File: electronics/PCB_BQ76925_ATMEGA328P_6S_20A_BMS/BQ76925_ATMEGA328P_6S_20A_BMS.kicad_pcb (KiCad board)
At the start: 2 copper layers, 47 x 90 mm, 79 parts, among them J1 Conn_01x01, J2 Conn_01x01, J3 Conn_01x09, J4 Conn_01x02, J5 Conn_02x03, J6 Conn_01x04, Q1 BC817, Q2 IRFB4110, Q3 IRFB4110, Q4 IRFB4110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

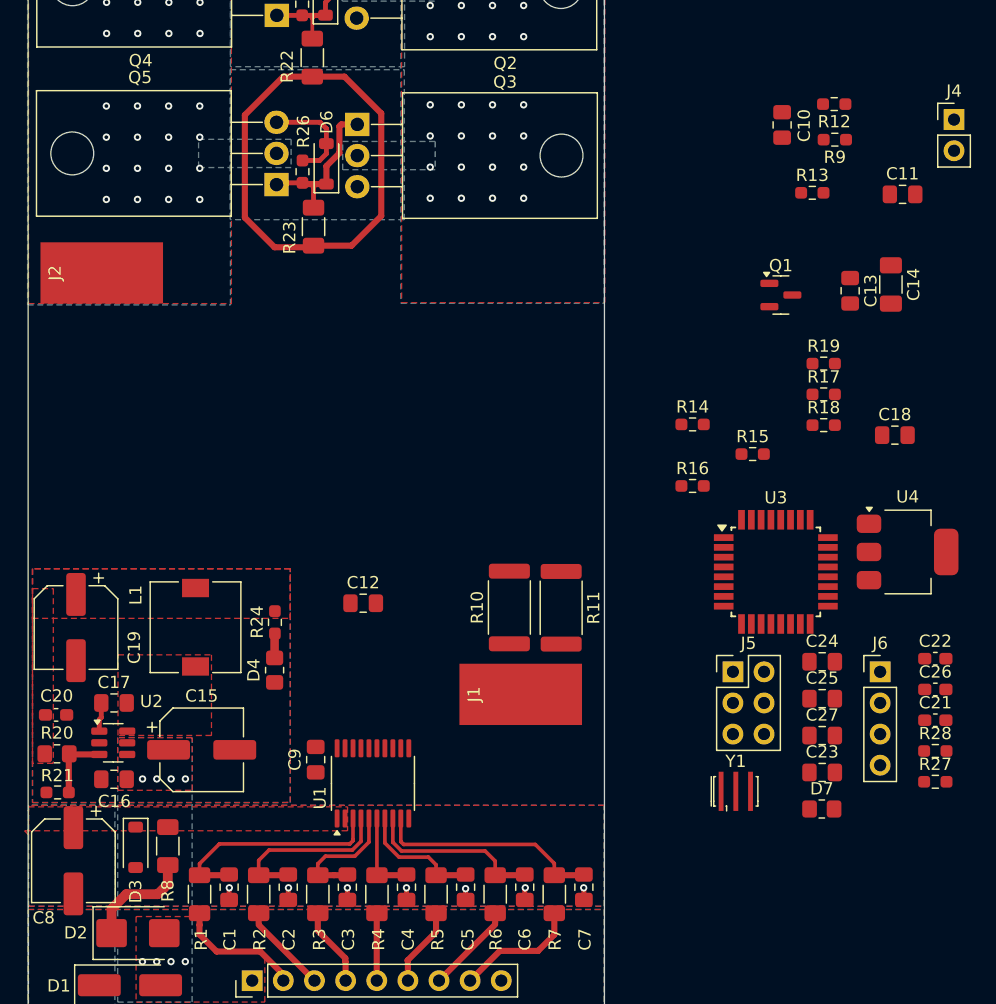
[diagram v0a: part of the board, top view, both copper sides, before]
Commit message: routing issue analog pins parallel routing and more length need to plan
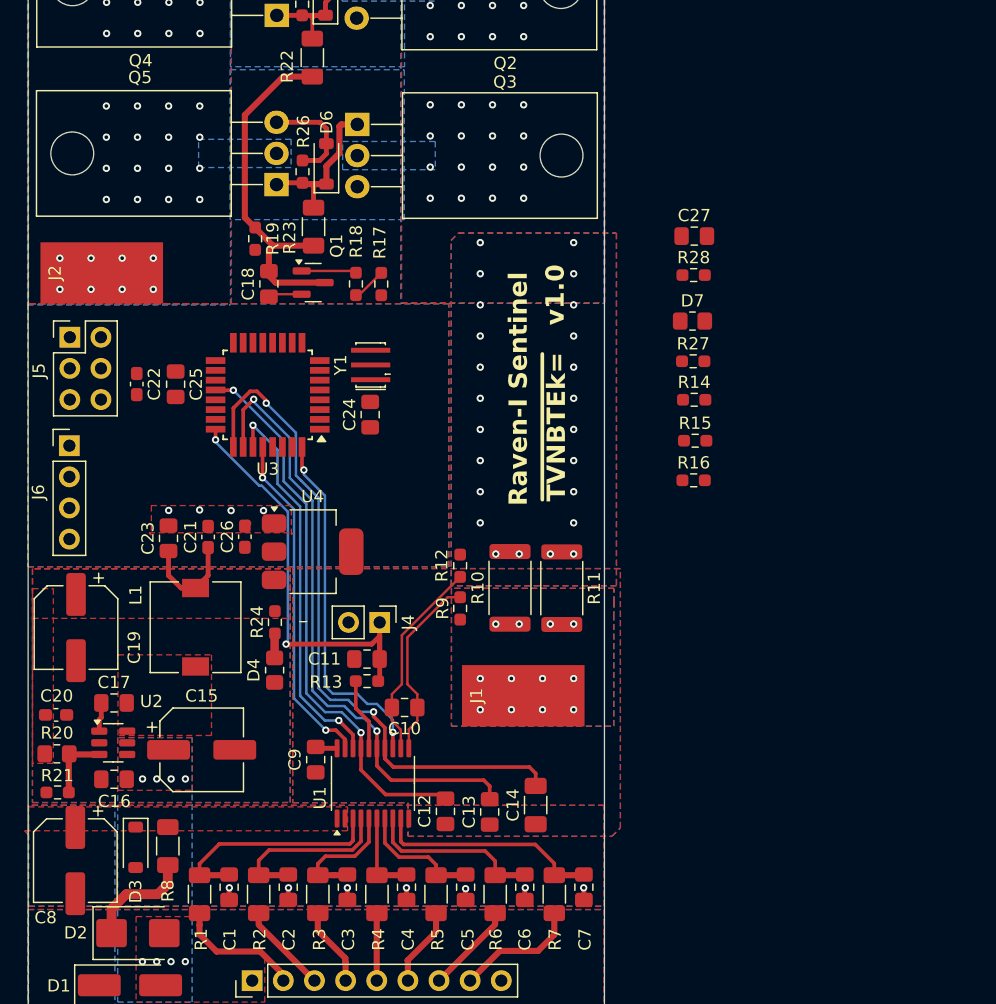
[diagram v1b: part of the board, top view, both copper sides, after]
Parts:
- moved C22 68.9 mm to (124.4, 87.7), turned to -90 degrees
- moved J6 68.7 mm to (118.9, 92.8)
- moved J4 62.3 mm to (144.2, 107.2), turned to -90 degrees
- moved C21 61.2 mm to (130.2, 100.2), turned to 90 degrees
- moved J5 60.6 mm to (118.9, 83.9)
- moved C25 58.6 mm to (127.5, 87.8), turned to -90 degrees
- moved C11 57.8 mm to (143.2, 110.2)
- moved C26 57.7 mm to (133.2, 100.2), turned to 90 degrees
- moved C23 56.6 mm to (127.0, 100.3), turned to 90 degrees
- moved C10 56.6 mm to (146.2, 114.1), turned to 180 degrees
- moved R13 53.9 mm to (143.2, 112.0), turned to 180 degrees
- moved C18 52.5 mm to (135.2, 79.6), turned to -90 degrees
- moved C13 51.7 mm to (153.2, 122.6), turned to 90 degrees
- moved C14 51.4 mm to (156.9, 122.1), turned to 90 degrees
- moved R9 48.9 mm to (150.8, 106.0), turned to 90 degrees
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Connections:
- net Net-(U1-SENSEN) renamed /24V 6 Cell Monitoring/A+
- net Net-(U1-SENSEP) renamed /24V 6 Cell Monitoring/A-
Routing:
- net /24V 6 Cell Monitoring/VIOUT: track 0.00 -> 55.3 mm, vias 0 -> 2
- net /24V 6 Cell Monitoring/VCOUT: track 0.00 -> 50.5 mm, vias 0 -> 2
- net /24V 6 Cell Monitoring/VREF: track 0.00 -> 45.4 mm, vias 0 -> 2
- net /24V 6 Cell Monitoring/VTB: track 0.00 -> 34.8 mm, vias 0 -> 2
- net /24V 6 Cell Monitoring/SDA: track 0.00 -> 32.2 mm, vias 0 -> 2
- net /24V 6 Cell Monitoring/ALERT: track 0.00 -> 29.3 mm, vias 0 -> 2
- net /24V 6 Cell Monitoring/SCL: track 0.00 -> 27.9 mm, vias 0 -> 2
- net /24V 6 Cell Monitoring/A-: track 0.00 -> 16.6 mm
- net /24V 6 Cell Monitoring/A+: track 0.00 -> 15.3 mm
- net Net-(Q1-C): track 43.6 -> 29.1 mm
- net +12V: track 0.00 -> 8.35 mm
- net Net-(U1-VTB): track 0.00 -> 5.92 mm
- net Net-(Q1-B): track 0.00 -> 4.49 mm
- net GND: track 6.88 -> 9.98 mm, vias 7 -> 11
- net /MCU/SW: track 0.00 -> 2.82 mm
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- added copper zone on F.Cu, net +5V
- added copper zone on B.Cu, net /24V 6 Cell Monitoring/BAT-
- added copper zone on F.Cu, net /24V 6 Cell Monitoring/BAT-
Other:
- board text added: "Raven-I Sentinel"
- board text added: "v1.0"
- board text added: "~{TVNBTEk=}"

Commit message: pcb placement and 90 percent routed
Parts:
- moved R14 45.8 mm to (137.0, 120.9), turned to 180 degrees
- moved C27 43.1 mm to (154.1, 115.8)
- moved J6 42.1 mm to (158.3, 107.6)
- moved R15 41.8 mm to (137.0, 118.0), turned to 180 degrees
- moved D7 40.4 mm to (131.5, 95.5), turned to -90 degrees
- moved R28 38.9 mm to (134.7, 95.6), turned to -90 degrees
- moved J4 28.2 mm to (117.9, 96.9), turned to 0 degrees
- moved R27 26.5 mm to (143.8, 90.7), turned to 180 degrees
- moved C11 25.4 mm to (120.9, 97.9), turned to 90 degrees
- moved C22 25.2 mm to (138.2, 108.8)
- moved C25 24.9 mm to (140.3, 109.2)
- moved R13 24.8 mm to (122.7, 97.9), turned to -90 degrees
- moved U3 24.1 mm to (146.7, 109.8)
- moved R16 24.0 mm to (154.2, 113.8)
- moved J1 23.3 mm to (155.9, 89.9)
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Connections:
- J5 pad 2: /MCU/SCK -> +5V
- J5 pad 3: /MCU/~{RESET} -> /MCU/SCK
- J5 pad 4: GND -> /MCU/MOSI
- J5 pad 5: /MCU/MOSI -> /MCU/~{RESET}
- J5 pad 6: +5V -> GND
- U3 pad 25: /24V 6 Cell Monitoring/VIOUT -> /24V 6 Cell Monitoring/VCOUT
- U3 pad 26: /24V 6 Cell Monitoring/VCOUT -> /24V 6 Cell Monitoring/VIOUT
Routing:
- net +5V: track 0.00 -> 80.0 mm
- net /24V 6 Cell Monitoring/VIOUT: track 55.3 -> 17.4 mm, vias 2 -> 0
- net /24V 6 Cell Monitoring/VCOUT: track 50.5 -> 15.8 mm, vias 2 -> 0
- net /MCU/~{RESET}: track 0.00 -> 32.6 mm, vias 0 -> 2
- net +12V: track 8.35 -> 32.2 mm
- net Net-(U1-VTB): track 5.92 -> 28.7 mm, vias 0 -> 2
- net /24V 6 Cell Monitoring/A+: track 15.3 -> 37.9 mm
- net /24V 6 Cell Monitoring/A-: track 16.6 -> 38.8 mm
- net /24V 6 Cell Monitoring/SDA: track 32.2 -> 13.2 mm, vias 2 -> 4
- net /24V 6 Cell Monitoring/ALERT: track 29.3 -> 11.2 mm
- net /24V 6 Cell Monitoring/VREF: track 45.4 -> 29.3 mm, vias 2 -> 0
- net /MCU/RXD: track 0.00 -> 14.2 mm, vias 0 -> 1
- net /MCU/MOSI: track 0.00 -> 13.8 mm
- net /MCU/MISO: track 0.00 -> 13.4 mm, vias 0 -> 1
- net /MCU/SCK: track 0.00 -> 12.6 mm
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- removed copper zone on F.Cu, net +5V
- removed copper zone on B.Cu, net /24V 6 Cell Monitoring/BAT-
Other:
- board size 47 x 90 mm -> 47 x 84 mm

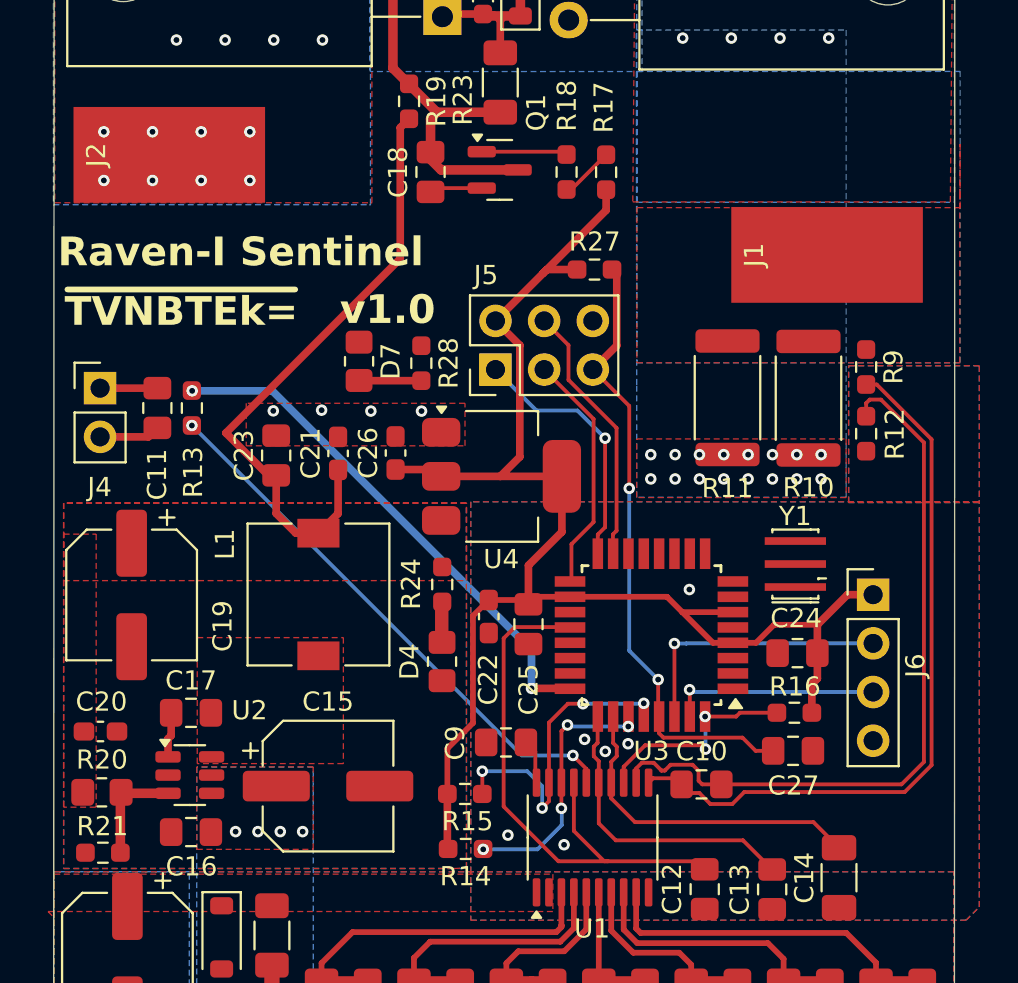
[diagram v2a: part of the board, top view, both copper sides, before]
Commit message: PCB DRC complete footprints library exported. PCB optimization required
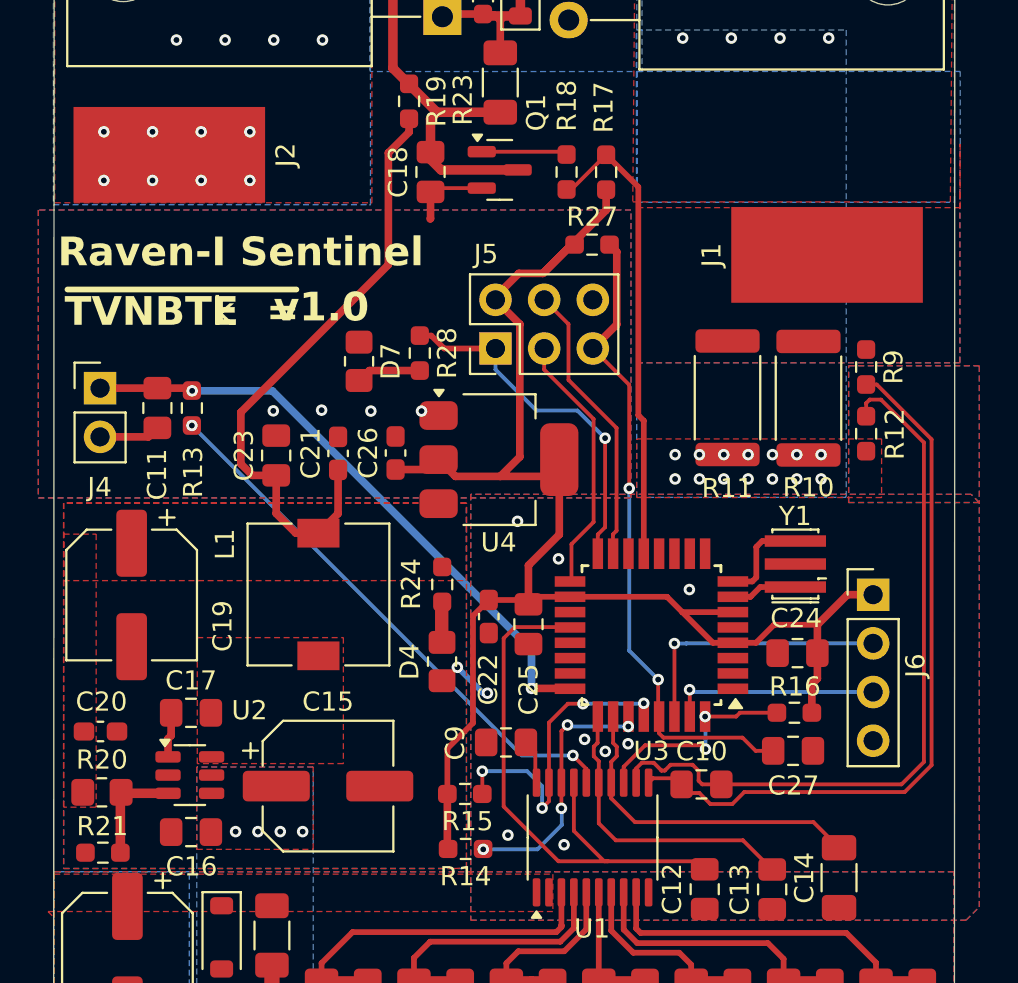
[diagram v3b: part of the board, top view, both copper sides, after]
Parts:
- C1, C10, C11, C12, C13, C16, C17, C18, C2, C23, C24, C25, C27, C3, C4, C5, C6, C7, C9: footprint Capacitor_SMD:C_0805_2012Metric_Pad1.18x1.45mm_HandSolder -> BQ76925_ATMEGA328P_6S_20A_BMS:C_0805_2012Metric_Pad1.18x1.45mm_HandSolder
- C14: footprint Capacitor_SMD:C_1206_3216Metric_Pad1.33x1.80mm_HandSolder -> BQ76925_ATMEGA328P_6S_20A_BMS:C_1206_3216Metric_Pad1.33x1.80mm_HandSolder
- C15, C19, C8: footprint Capacitor_SMD:CP_Elec_6.3x5.7 -> BQ76925_ATMEGA328P_6S_20A_BMS:CP_Elec_6.3x5.7
- C20, C21, C22, C26: footprint Capacitor_SMD:C_0603_1608Metric_Pad1.08x0.95mm_HandSolder -> BQ76925_ATMEGA328P_6S_20A_BMS:C_0603_1608Metric_Pad1.08x0.95mm_HandSolder
- D1: footprint Diode_SMD:D_SMA_Handsoldering -> BQ76925_ATMEGA328P_6S_20A_BMS:D_SMA_Handsoldering
- D2: footprint Diode_SMD:D_SMB -> BQ76925_ATMEGA328P_6S_20A_BMS:D_SMB
- D3, D5, D6: footprint Diode_SMD:D_SOD-123 -> BQ76925_ATMEGA328P_6S_20A_BMS:D_SOD-123
- D4, D7, R20: footprint Resistor_SMD:R_0805_2012Metric_Pad1.20x1.40mm_HandSolder -> BQ76925_ATMEGA328P_6S_20A_BMS:R_0805_2012Metric_Pad1.20x1.40mm_HandSolder
- J1, J2: footprint Connector_Wire:SolderWirePad_1x01_SMD_5x10mm -> BQ76925_ATMEGA328P_6S_20A_BMS:SolderWirePad_1x01_SMD_5x10mm
- J3: footprint Connector_PinHeader_2.54mm:PinHeader_1x09_P2.54mm_Vertical -> BQ76925_ATMEGA328P_6S_20A_BMS:PinHeader_1x09_P2.54mm_Vertical
- J4: footprint Connector_PinHeader_2.54mm:PinHeader_1x02_P2.54mm_Vertical -> BQ76925_ATMEGA328P_6S_20A_BMS:PinHeader_1x02_P2.54mm_Vertical
- J5: footprint Connector_PinHeader_2.54mm:PinHeader_2x03_P2.54mm_Vertical -> BQ76925_ATMEGA328P_6S_20A_BMS:PinHeader_2x03_P2.54mm_Vertical
- J6: footprint Connector_PinHeader_2.54mm:PinHeader_1x04_P2.54mm_Vertical -> BQ76925_ATMEGA328P_6S_20A_BMS:PinHeader_1x04_P2.54mm_Vertical
- L1: footprint Inductor_SMD:L_7.3x7.3_H3.5 -> BQ76925_ATMEGA328P_6S_20A_BMS:L_7.3x7.3_H3.5
- Q1: footprint Package_TO_SOT_SMD:SOT-23 -> BQ76925_ATMEGA328P_6S_20A_BMS:SOT-23
- Q2, Q3, Q4, Q5: footprint Package_TO_SOT_THT:TO-220-3_Horizontal_TabDown -> BQ76925_ATMEGA328P_6S_20A_BMS:TO-220-3_Horizontal_TabDown
- R1, R2, R22, R23, R3, R4, R5, R6, R7, R8: footprint Resistor_SMD:R_1206_3216Metric_Pad1.30x1.75mm_HandSolder -> BQ76925_ATMEGA328P_6S_20A_BMS:R_1206_3216Metric_Pad1.30x1.75mm_HandSolder
- R10, R11: footprint Resistor_SMD:R_2512_6332Metric -> BQ76925_ATMEGA328P_6S_20A_BMS:R_2512_6332Metric
- R12, R13, R14, R15, R16, R17, R18, R19, R21, R24, R25, R26, R27, R28, R9: footprint Resistor_SMD:R_0603_1608Metric_Pad0.98x0.95mm_HandSolder -> BQ76925_ATMEGA328P_6S_20A_BMS:R_0603_1608Metric_Pad0.98x0.95mm_HandSolder
- U1: footprint Package_SO:TSSOP-20_4.4x6.5mm_P0.65mm -> BQ76925_ATMEGA328P_6S_20A_BMS:TSSOP-20_4.4x6.5mm_P0.65mm
- U2: footprint Package_TO_SOT_SMD:SOT-23-6 -> BQ76925_ATMEGA328P_6S_20A_BMS:SOT-23-6
- U3: footprint Package_QFP:TQFP-32_7x7mm_P0.8mm -> BQ76925_ATMEGA328P_6S_20A_BMS:TQFP-32_7x7mm_P0.8mm
- U4: footprint Package_TO_SOT_SMD:SOT-223-3_TabPin2 -> BQ76925_ATMEGA328P_6S_20A_BMS:SOT-223-3_TabPin2
- Y1: footprint Crystal:Resonator_SMD_Murata_CSTxExxV-3Pin_3.0x1.1mm_HandSoldering -> BQ76925_ATMEGA328P_6S_20A_BMS:Resonator_SMD_Murata_CSTxExxV-3Pin_3.0x1.1mm_HandSoldering
- moved R27 1.31 mm to (143.6, 89.4)
- moved J5 1.10 mm to (138.6, 94.8)
- moved U4 0.89 mm to (138.8, 100.6)
- moved R28 0.53 mm to (134.6, 95.0)
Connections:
- R28 pad 1: /MCU/SCK -> /MCU/MISO
- U3 pad 1: /MCU/SW -> unconnected-(U3-PD3-Pad1)
- U3 pad 13: unconnected-(U3-PB1-Pad13) -> /MCU/SW
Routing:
- net /MCU/SW: track 2.82 -> 24.5 mm
- net /MCU/MISO: track 13.4 -> 18.7 mm
- net /MCU/XTAL2: track 0.00 -> 5.07 mm
- net GND: track 12.8 -> 16.4 mm, vias 17 -> 21
- net /MCU/XTAL1: track 0.00 -> 3.47 mm
- net +5V: track 80.0 -> 82.6 mm
- net /24V 6 Cell Monitoring/VTB: track 30.3 -> 32.2 mm
- net /MCU/~{RESET}: track 32.6 -> 33.9 mm
- net /MCU/MOSI: track 13.8 -> 14.9 mm
- net /MCU/SCK: track 12.6 -> 13.7 mm
- net /24V 6 Cell Monitoring/PACK-: vias 48 -> 46
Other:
- board text added: "k"
- board text added: "~{TVNBTE =}"
- board text removed: "~{TVNBTEk=}"
